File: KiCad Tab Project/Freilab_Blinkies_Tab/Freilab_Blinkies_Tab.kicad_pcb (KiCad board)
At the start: 2 copper layers, 6 x 11.2 mm, 2 parts

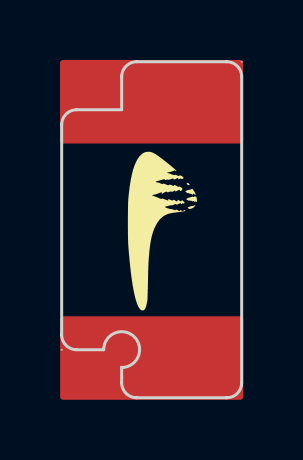
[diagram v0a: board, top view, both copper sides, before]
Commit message: fix corners
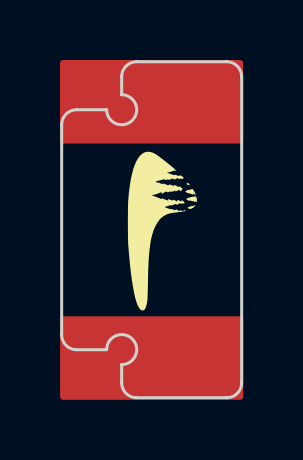
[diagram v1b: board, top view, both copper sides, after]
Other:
- outline, holes or cut-outs redrawn
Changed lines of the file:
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@@
 		(layer "F.Cu")
 	)
-	(gr_rect
-		(start 135.044124 69.947064)
-		(end 140.949991 72.530435)
+	(gr_poly
+		(pts
+			(xy 135.044124 69.947064) (xy 140.949991 69.947064) (xy 140.949991 72.530435) (xy 135.044124 72.530435)
+		)
 		(stroke
 			(width 0.2)
@@
 	)
 	(gr_line
-		(start 137 71.505385)
+		(start 137 71.005356)
 		(end 137 70.405385)
 		(stroke
@@
 	)
 	(gr_arc
-		(start 136.402902 79.505387)
-		(mid 137.42032 79.07587)
-		(end 137 80.097122)
+		(start 136.50002 79.504511)
+		(mid 137.351955 79.144855)
+		(end 137 80)
+		(stroke
+			(width 0.1)
+			(type solid)
+		)
+		(layer "Edge.Cuts")
+	)
+	(gr_arc
+		(start 137 71.005356)
+		(mid 137.353574 71.858959)
+		(end 136.499971 71.505385)
 		(stroke
 			(width 0.1)
@@
 	(gr_line
 		(start 135.5 71.505385)
-		(end 137 71.505385)
+		(end 136.5 71.505385)
 		(stroke
 			(width 0.1)
 			(type default)
 		)
-		(layer "Edge.Cuts")
-	)
-	(gr_circle
-		(center 135 79.505385)
-		(end 135.01 79.505385)
-		(stroke
-			(width 0.0001)
-			(type default)
-		)
-		(fill yes)
 		(layer "Edge.Cuts")
 	)
@@
 	)
 	(gr_line
-		(start 136.402902 79.505387)
+		(start 136.5 79.505387)
 		(end 135.499971 79.505385)
 		(stroke
@@
 	(gr_line
 		(start 137 80.6)
-		(end 137 80.086959)
+		(end 137 80)
 		(stroke
 			(width 0.1)
@@
 		(layer "Edge.Cuts")
 	)
-	(gr_circle
-		(center 141 69.905385)
-		(end 141.01 69.905385)
-		(stroke
-			(width 0.0001)
-			(type default)
-		)
-		(fill yes)
-		(layer "Edge.Cuts")
-	)
